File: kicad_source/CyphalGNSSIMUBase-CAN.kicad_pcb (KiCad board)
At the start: 2 copper layers, 52 x 36 mm, 62 parts, among them CN1 RASPBERRYPI_PICO, CN12 S3B-PH-SM4-TB, CN2 SM04B-SRSS-TB, CN3 SM04B-SRSS-TB, CN4 SM04B-GHS-TB, CN5 SM04B-GHS-TB, CN7 DNI, CN8 DNI, SW1 PTS636 SM43 SMTR LFS, U3 M24C64-RMN6TP, U8 MCP2515T-I/SO, U9 SN65HVD230, Y1 X322516MLB4SI

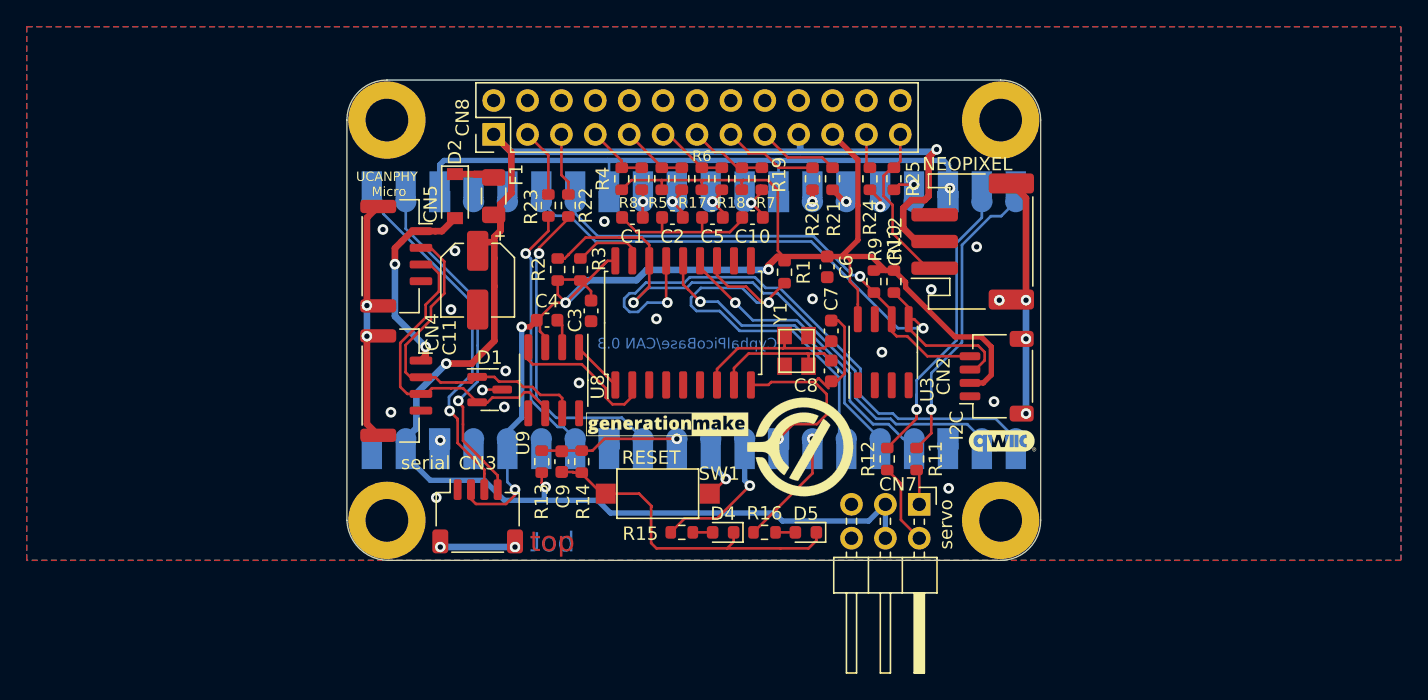
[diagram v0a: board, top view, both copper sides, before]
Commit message: removed unnecessary parts
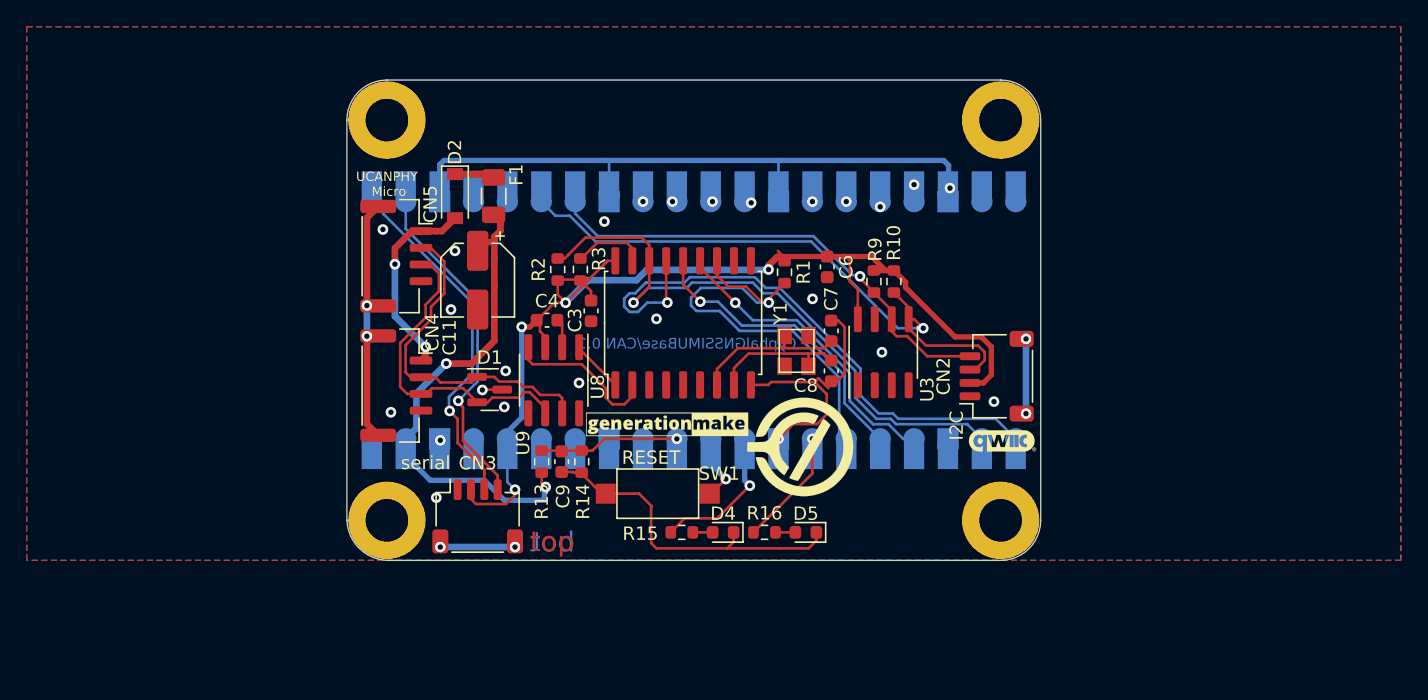
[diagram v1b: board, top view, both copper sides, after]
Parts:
- removed C1, C10, C2, C5: 100nF, Capacitor_SMD:C_0603_1608Metric
- removed CN12: S3B-PH-SM4-TB, generationmake:JST_PH_S3B-PH-SM4-TB_1x03-1MP_P2.00mm_Horizontal
- removed CN7: DNI, Connector_PinHeader_2.54mm:PinHeader_2x03_P2.54mm_Horizontal
- removed CN8: DNI, Connector_PinHeader_2.54mm:PinHeader_2x13_P2.54mm_Vertical
- removed R11, R12, R20, R21, R22, R23, R24, R25: 100R, Resistor_SMD:R_0603_1608Metric
- removed R17, R18, R19, R4, R5, R6, R7, R8: 10k, Resistor_SMD:R_0603_1608Metric
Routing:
- net +BATT: track 120.7 -> 37.9 mm, vias 3 -> 2
- net +3V3: track 113.3 -> 83.8 mm
- net /ANALOG_INPUT0: track 25.1 -> 1.27 mm, vias 1 -> 0
- net /SERVO1: track 24.1 -> 1.27 mm, vias 1 -> 0
- net /SERVO0: track 23.4 -> 1.27 mm, vias 1 -> 0
- net /ANALOG_INPUT1: track 20.4 -> 1.27 mm, vias 1 -> 0
- net /MP2: track 19.7 -> 5.60 mm, vias 4 -> 2
- net /NEOPIXEL_R: track 12.6 -> 0.00 mm
- net GND: track 106.9 -> 94.6 mm, vias 20 -> 17
- net /OUTPUT0_R: track 7.22 -> 0.00 mm
- net (no net): track 0.00 -> 6.35 mm
- net /OUTPUT1_R: track 6.12 -> 0.00 mm
- net /SERVO0_R: track 6.11 -> 0.00 mm
- net /INPUT3_R: track 5.90 -> 0.00 mm
- net /INPUT2_R: track 5.44 -> 0.00 mm
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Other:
- board text added: "CyphalGNSSIMUBase/CAN 0.1"
- board text added: "find data and documentation at https://github.com/generationmake/CyphalGNSSIMUBase-CAN"
- board text removed: "+3V3"
- board text removed: "ANALOG0"
- board text removed: "ANALOG1"
- board text removed: "CyphalPicoBase/CAN 0.3"
- board text removed: "INPUT0"
- board text removed: "INPUT1"
- board text removed: "INPUT2"
- board text removed: "INPUT3"
- board text removed: "NEOPIXEL"
- board text removed: "OUTPUT0"
- board text removed: "OUTPUT1"
- board text removed: "RESERVED0"
- board text removed: "SERVO0"
- board text removed: "SERVO1"
- board text removed: "T | + | -"
- board text removed: "V_IN"
- board text removed: "find data and documentation at https://github.com/generationmake/CyphalPicoBase-CAN"
- board text removed: "servo"
